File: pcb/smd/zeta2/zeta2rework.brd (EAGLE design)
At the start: 121.6 x 87.6 mm, 113 parts, among them IC1 MAX6520, IC2 L293DD, IC3 L293DD, Q12 8MHz, U1 MPU-6050, U2 INA219, U4 INA219, U5 DS18B20U+

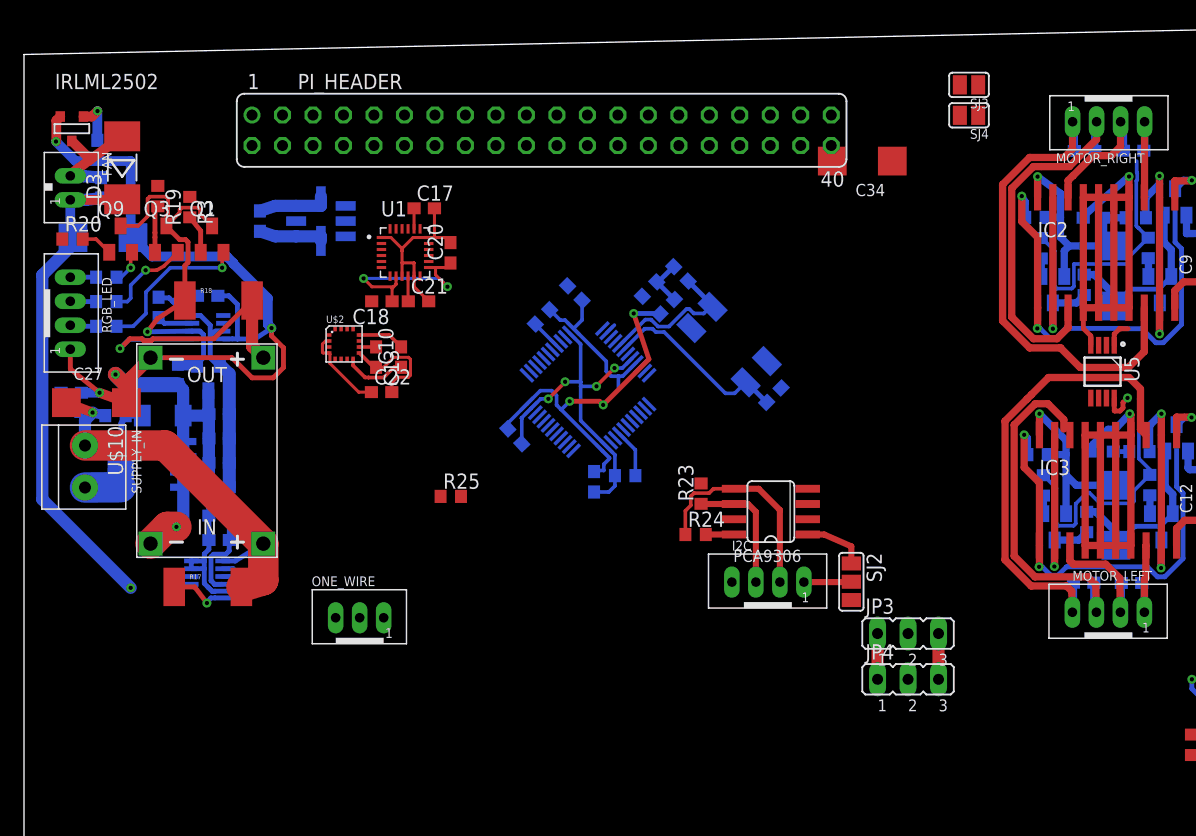
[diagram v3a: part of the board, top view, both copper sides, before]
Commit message: worked on pcb layout -piheader wrong
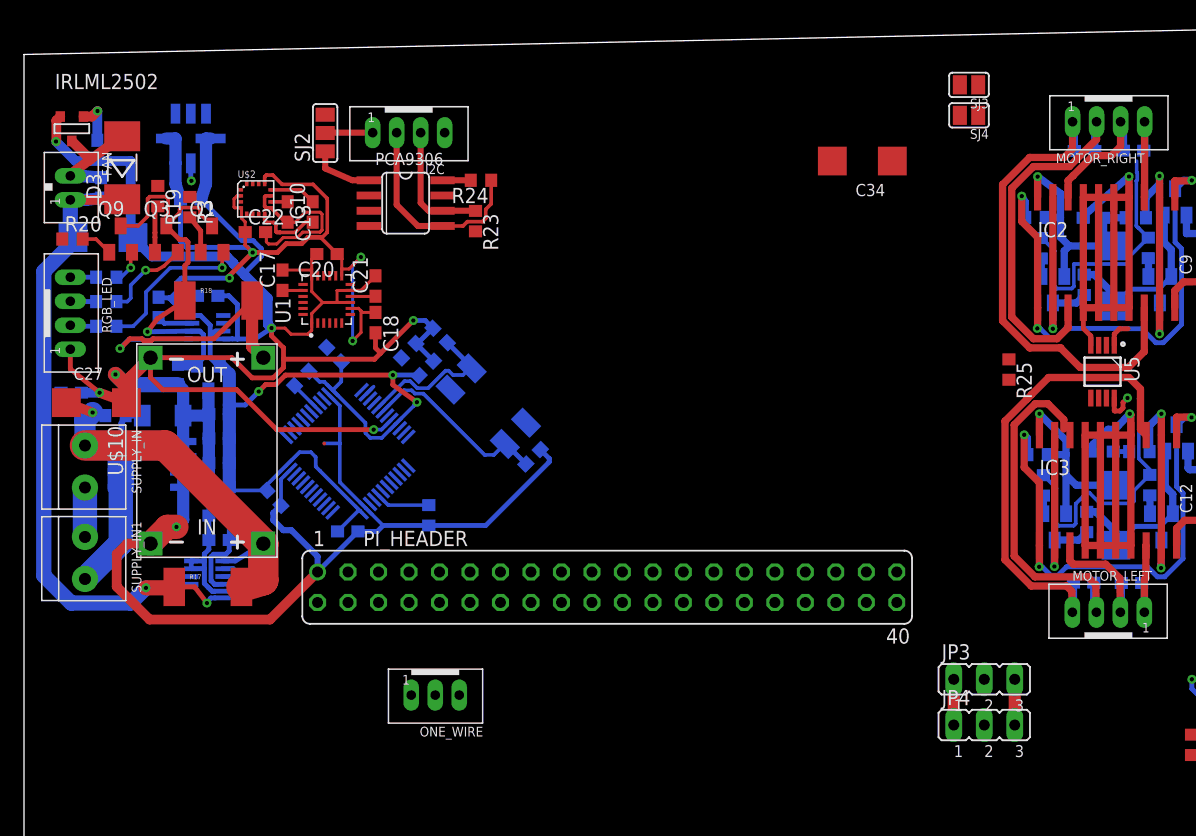
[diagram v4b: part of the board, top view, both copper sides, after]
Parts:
- added SUPPLY_IN1: TERMBLOCK_1X2-3.5MM, microbuilder:1X2-3.5MM
- moved SJ2 57.6 mm to (23.8, 73.5), turned to 90 degrees
- moved I2C 48.0 mm to (30.8, 73.5), turned to 180 degrees
- moved R25 47.7 mm to (80.8, 53.7), turned to 270 degrees
- moved PCA9306 39.8 mm to (30.5, 67.6), turned to 270 degrees
- moved PI_HEADER 38.5 mm to (47.3, 35.6)
- moved R24 34.5 mm to (36.8, 69.5), turned to 180 degrees
- moved R23 29.5 mm to (36.3, 66.1), turned to 270 degrees
- moved C38 20.9 mm to (25.7, 40.3), turned to 180 degrees
- moved C33 20.7 mm to (19.6, 43.1)
- moved Q12 20.7 mm to (37.4, 50.7)
- moved R31 20.7 mm to (21.9, 53.0)
- moved C40 20.7 mm to (24.6, 55.0)
- moved R30 20.7 mm to (30.8, 55.3)
- moved U$4 20.7 mm to (25.7, 46.9)
- moved C36 20.7 mm to (41.1, 46.5)
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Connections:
- new net N$50: SUPPLY_IN.1, SUPPLY_IN1.2
- net N$60: now also SUPPLY_IN1.1; no longer SUPPLY_IN.1
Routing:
- net GND: track 327.1 -> 431.3 mm, vias 11 -> 9
- net +3V3: track 121.7 -> 165.0 mm, vias 6 -> 8
- net +8V: track 63.1 -> 71.3 mm
- net N$60: track 5.53 -> 11.4 mm
- net N$50: track 0.00 -> 4.12 mm
- net BMP_EOC: track 0.00 -> 1.49 mm, vias 0 -> 1
- net N$39: track 5.29 -> 5.92 mm

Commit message: added hall effect sensor
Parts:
- added C19, C30, C32, C35, C42, C44: 4.7nF, rcl:C0603
- added R29, R32, R34: 1.2k, rcl:R0603
- added TLE4905L, TLE4905L1, TLE4905L2: JST-PH_3-PIN_HEADER, srg:JST_B3B-PH_HEADER
- moved SJ2 58.6 mm to (55.0, 23.9), turned to 270 degrees
- moved I2C 52.7 mm to (48.1, 23.8), turned to 0 degrees
- moved C34 50.1 mm to (18.7, 66.3), turned to 270 degrees
- moved R24 42.0 mm to (42.0, 27.8), turned to 0 degrees
- moved PCA9306 41.8 mm to (48.3, 29.7), turned to 90 degrees
- moved R23 35.4 mm to (42.5, 31.2), turned to 90 degrees
- moved PI_HEADER 30.4 mm to (46.7, 66.0), turned to 180 degrees
- moved SJ4 26.9 mm to (58.4, 55.9)
- moved SJ3 26.9 mm to (58.4, 58.4)
- moved Q10 21.2 mm to (102.6, 47.7)
- moved Q11 21.2 mm to (102.6, 43.7)
- moved R15 21.2 mm to (102.7, 50.7)
- moved R16 21.2 mm to (103.6, 44.2)
- moved R4 21.2 mm to (103.6, 46.2)
- moved LED 21.2 mm to (106.8, 46.3)
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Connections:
- new net HALL_1: C30.2, R29.1, TLE4905L.P3
- new net HALL_2: C35.2, R32.1, TLE4905L1.P3
- new net HALL_3: C44.2, R34.1, TLE4905L2.P3
- net +5V: now also C19.1, C32.1, C42.1, R29.2, R32.2, R34.2, TLE4905L.P1, TLE4905L1.P1, TLE4905L2.P1
- net GND: now also C19.2, C30.1, C32.2, C35.1, C42.2, C44.1, TLE4905L.P2, TLE4905L1.P2, TLE4905L2.P2
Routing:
- net +5V: track 75.2 -> 97.5 mm
- net GND: track 431.3 -> 443.9 mm, vias 9 -> 10
- net HALL_3: track 0.00 -> 7.48 mm
- net HALL_2: track 0.00 -> 7.46 mm
- net HALL_1: track 0.00 -> 7.28 mm
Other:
- board size 121.6 x 87.6 mm -> 122.9 x 80 mm

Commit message: worked on layout
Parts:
- moved U$2 34.9 mm to (53.1, 51.4), turned to 180 degrees
- moved C22 34.0 mm to (53.1, 54.2), turned to 180 degrees
- moved ONE_WIRE 34.0 mm to (67.8, 24.4), turned to 0 degrees
- moved C15 32.8 mm to (45.8, 52.5), flipped to the top, turned to 270 degrees
- moved U$3 29.7 mm to (40.7, 52.5), flipped to the top, turned to 180 degrees
- moved C13 29.2 mm to (50.4, 52.5), turned to 90 degrees
- moved SJ3 27.1 mm to (31.8, 53.3), turned to 90 degrees
- moved C10 25.2 mm to (48.3, 52.5), turned to 270 degrees
- moved SJ4 24.3 mm to (34.3, 53.3), turned to 90 degrees
- moved PI_HEADER 6.28 mm to (43.0, 60.9)
- moved C36 6.11 mm to (37.5, 35.2), turned to 0 degrees
- moved IRLML2502 5.30 mm to (8.00, 62.8)
- moved Q9 5.08 mm to (8.13, 51.9)
- moved R22 4.67 mm to (11.4, 63.8), flipped to the top, turned to 180 degrees
- moved D3 4.40 mm to (11.8, 60.5), flipped to the bottom, turned to 180 degrees
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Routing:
- net +3V3: track 165.0 -> 127.3 mm, vias 8 -> 6
- net +5V: track 97.5 -> 107.3 mm
- net GND: track 443.9 -> 435.6 mm
- net N$55: track 10.3 -> 16.7 mm, vias 0 -> 1
- net N$47: track 12.1 -> 18.3 mm
- net PWM_M_EN_1: track 0.00 -> 4.72 mm, vias 0 -> 1
- net PWM_M_EN_2: track 0.00 -> 4.71 mm, vias 0 -> 1
- net N$29: track 2.84 -> 6.14 mm
- net S_PWM_SPEED: track 0.00 -> 3.03 mm, vias 0 -> 1
- net S_DIR: track 0.00 -> 2.87 mm, vias 0 -> 1
- net M_DIR_1: track 22.4 -> 25.3 mm, vias 0 -> 1
- net USART2_TX: track 0.00 -> 2.50 mm, vias 0 -> 1
- net N$37: track 3.80 -> 1.56 mm, vias 1 -> 0
- net USART2_RX: track 0.00 -> 2.07 mm, vias 0 -> 1
- net +8V: track 71.3 -> 69.8 mm
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
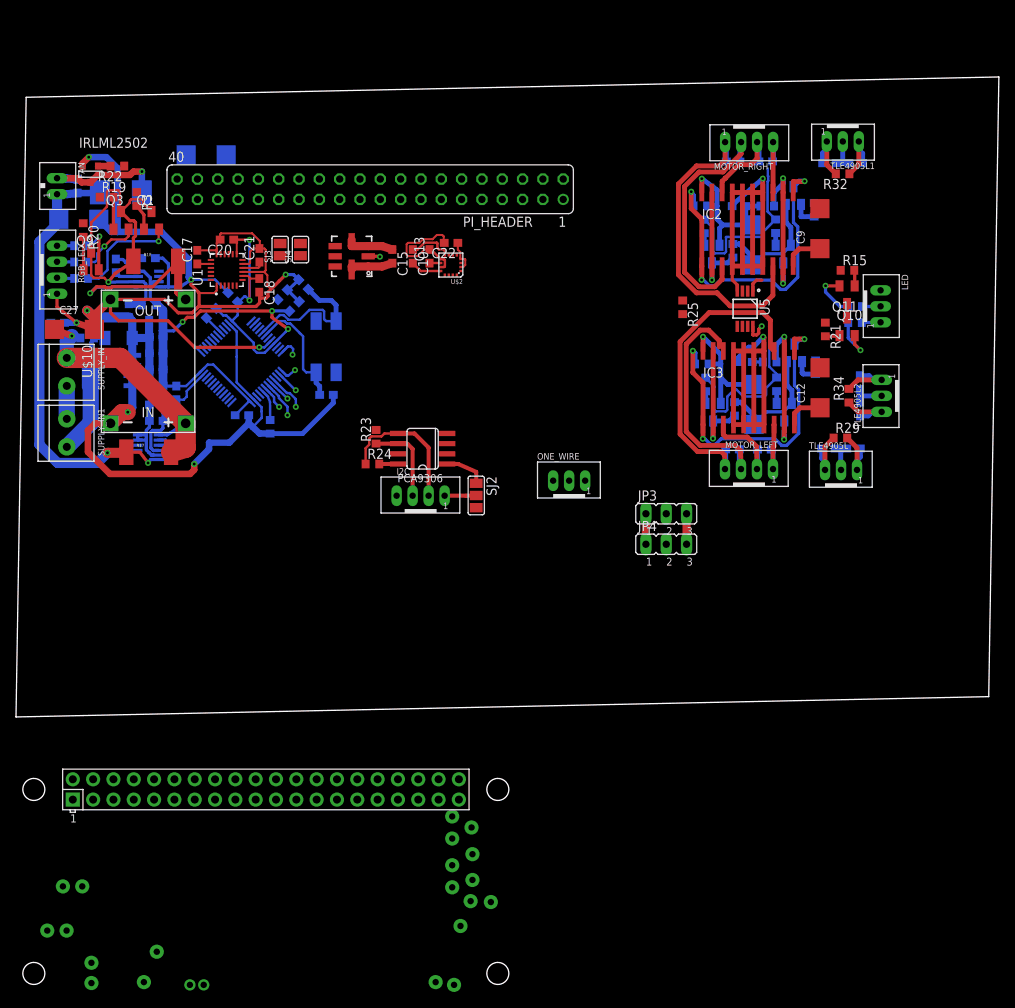
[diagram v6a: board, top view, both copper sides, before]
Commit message: adde capicator for mp6500
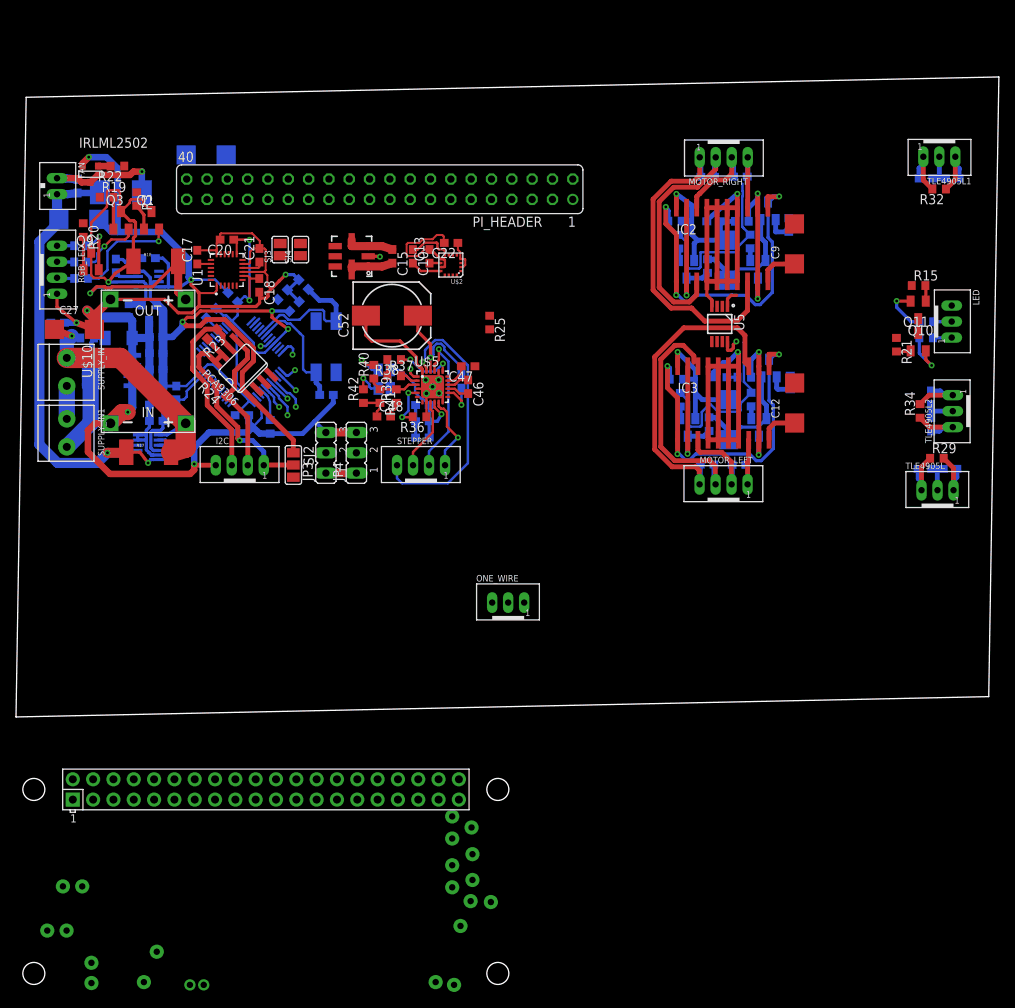
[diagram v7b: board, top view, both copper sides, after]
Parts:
- added C45: 1µf, rcl:C0603
- added C46: 100nF, rcl:C0603
- added C47: 0.22µF, rcl:C0603
- added C48, C50, C51: 0.1µF, rcl:C0603
- added C49: 4.7µF, rcl:C0603
- added C52: (no value), rcl:150CLZ-0810
- added R36, R38: 100k, rcl:R0603
- added R37: 22R, rcl:R0603
- added R39: 137k, rcl:R0603
- added R40: 75k, rcl:R0603
- added R41: 130k, rcl:R0603
- added R42: 7.5k, rcl:R0603
- added SJ1, SJ5: (no value), microbuilder:SOLDERJUMPER_REFLOW_NOPASTE
- added STEPPER: JST-PH_4-PIN_HEADER, srg:JST_B4B-PH_HEADER
- added U$5: MP6500, mp6500:QFN24
- moved JP3 43.2 mm to (37.5, 27.9), turned to 90 degrees
- moved JP4 40.4 mm to (41.3, 27.9), turned to 90 degrees
- moved PCA9306 24.6 mm to (27.1, 38.5), turned to 45 degrees
- moved R25 24.2 mm to (57.9, 44.2)
- moved R23 24.2 mm to (23.2, 42.8), turned to 225 degrees
- moved SJ2 23.2 mm to (33.4, 26.4)
- moved I2C 22.9 mm to (26.7, 26.3)
- moved R24 20.9 mm to (24.4, 35.6), turned to 135 degrees
- moved ONE_WIRE 17.0 mm to (60.2, 9.17)
- moved TLE4905L 12.3 mm to (113.9, 23.2)
- moved C19 12.3 mm to (115.5, 25.9)
- moved C30 12.3 mm to (112.3, 25.9)
- moved R29 12.3 mm to (113.8, 27.3)
- moved R32 12.2 mm to (114.1, 60.9)
- moved C32 12.2 mm to (112.5, 62.2)
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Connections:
- new net N$51: C45.1, U$5.VCP
- new net N$52: R38.1, U$5.NSLEEP
- new net N$53: C46.2, U$5.CP2
- new net N$54: C46.1, U$5.CP1
- new net N$57: C47.2, U$5.VG
- new net N$58: R36.2, U$5.ROSC
- new net N$59: R37.2, U$5.NFAULT
- new net N$61: STEPPER.P1, U$5.BOUT2
- new net N$62: STEPPER.P2, U$5.AOUT2
- new net N$63: R39.2, R40.1, R41.1, U$5.ISET
- new net N$64: STEPPER.P3, U$5.BOUT1
- new net N$65: R40.2, SJ1.2
- new net N$66: R42.2, SJ5.2
- new net N$67: C48.1, R41.2, R42.1
- new net N$68: STEPPER.P4, U$5.AOUT1
- new net S_MS1: U$5.MS1
- new net S_MS2: U$5.MS2
- new net S_NENBL: U$5.NENBL
- new net S_SLEEP: R37.1, R38.2
- new net S_STEP: U$5.STEP
- net +5V: now also C45.2, C49.1, C50.1, C51.1, C52.+, SJ1.1, SJ5.1, U$5.VIN, U$5.VIN@1
- net GND: now also C47.1, C48.2, C49.2, C50.2, C51.2, C52.-, R36.1, R39.1, U$5.AGND, U$5.EXP, U$5.GND@1, U$5.GND@2, U$5.GND@3, U$5.GND@4
- net S_DIR: now also U$5.DIR
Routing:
- net N$68: track 0.00 -> 34.2 mm, vias 0 -> 1
- net +5V: track 107.3 -> 140.0 mm, vias 3 -> 5
- net +3V3: track 127.3 -> 149.9 mm
- net N$41: track 6.30 -> 28.2 mm, vias 0 -> 1
- net N$62: track 0.00 -> 19.0 mm, vias 0 -> 1
- net GND: track 435.6 -> 452.2 mm, vias 10 -> 15
- net N$42: track 10.7 -> 24.0 mm
- net N$61: track 0.00 -> 9.76 mm, vias 0 -> 1
- net N$64: track 0.00 -> 9.04 mm
- net N$52: track 0.00 -> 7.28 mm, vias 0 -> 2
- net N$63: track 0.00 -> 6.57 mm
- net N$58: track 0.00 -> 5.85 mm, vias 0 -> 2
- net N$51: track 0.00 -> 4.74 mm, vias 0 -> 1
- net N$65: track 0.00 -> 4.38 mm, vias 0 -> 1
- net N$66: track 0.00 -> 3.95 mm, vias 0 -> 1
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
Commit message: added new pcb version
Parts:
- moved ONE_WIRE 17.2 mm to (61.5, 26.3)
- moved C47 1.15 mm to (54.5, 39.6), turned to 270 degrees
- moved C45 0.53 mm to (54.1, 36.4)
- moved C46 0.13 mm to (55.1, 36.2)
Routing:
- net S_STEP: track 0.00 -> 2.62 mm
- net GND: track 452.2 -> 449.7 mm
- net S_NENBL: track 0.00 -> 1.52 mm
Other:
- board size 122.9 x 80 mm -> 121.6 x 81.3 mm
